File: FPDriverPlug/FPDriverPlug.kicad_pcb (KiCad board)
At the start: 2 copper layers, 21 x 59.1 mm, 3 parts, among them CN1 Conn_02x05_Odd_Even, CN2 Conn_02x20_Counter_Clockwise_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, U1 FP2800A

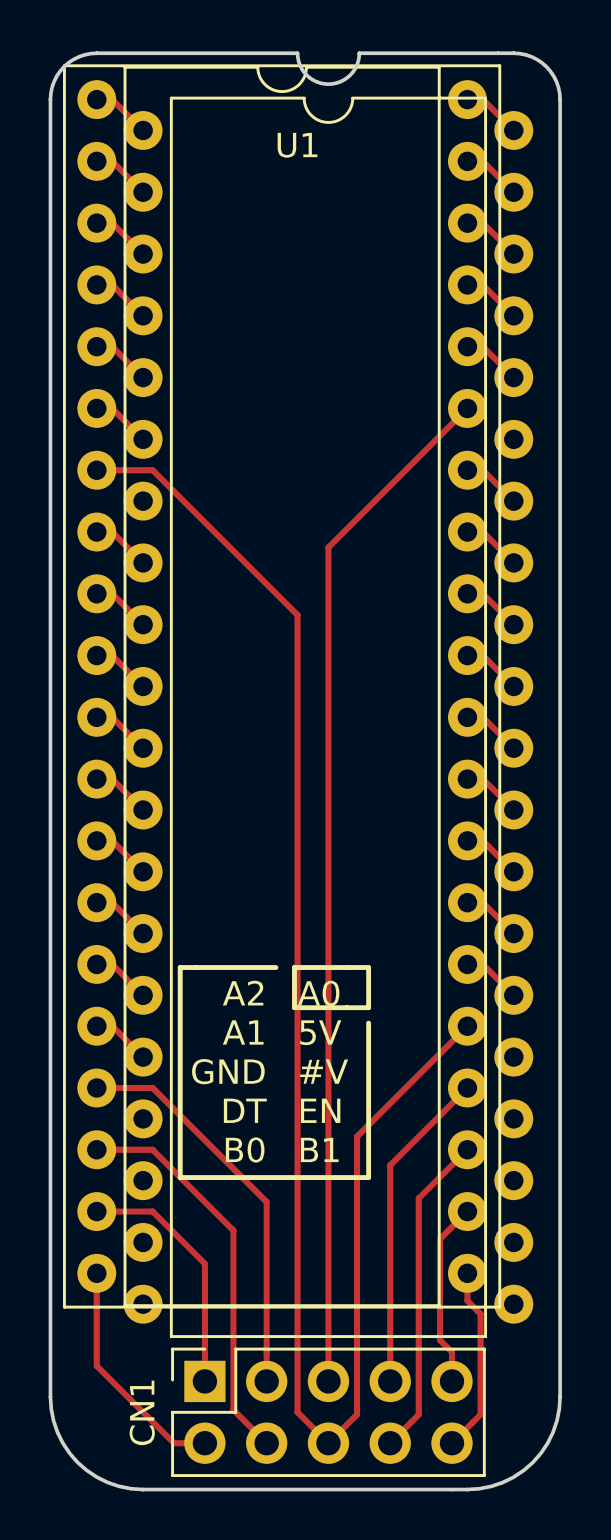
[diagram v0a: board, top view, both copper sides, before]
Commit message: Improve FPDriverPlug
- Switch from DIP40 to DIP32
- Use stronger traces for connections with relevant current
- Use copper fill for GND
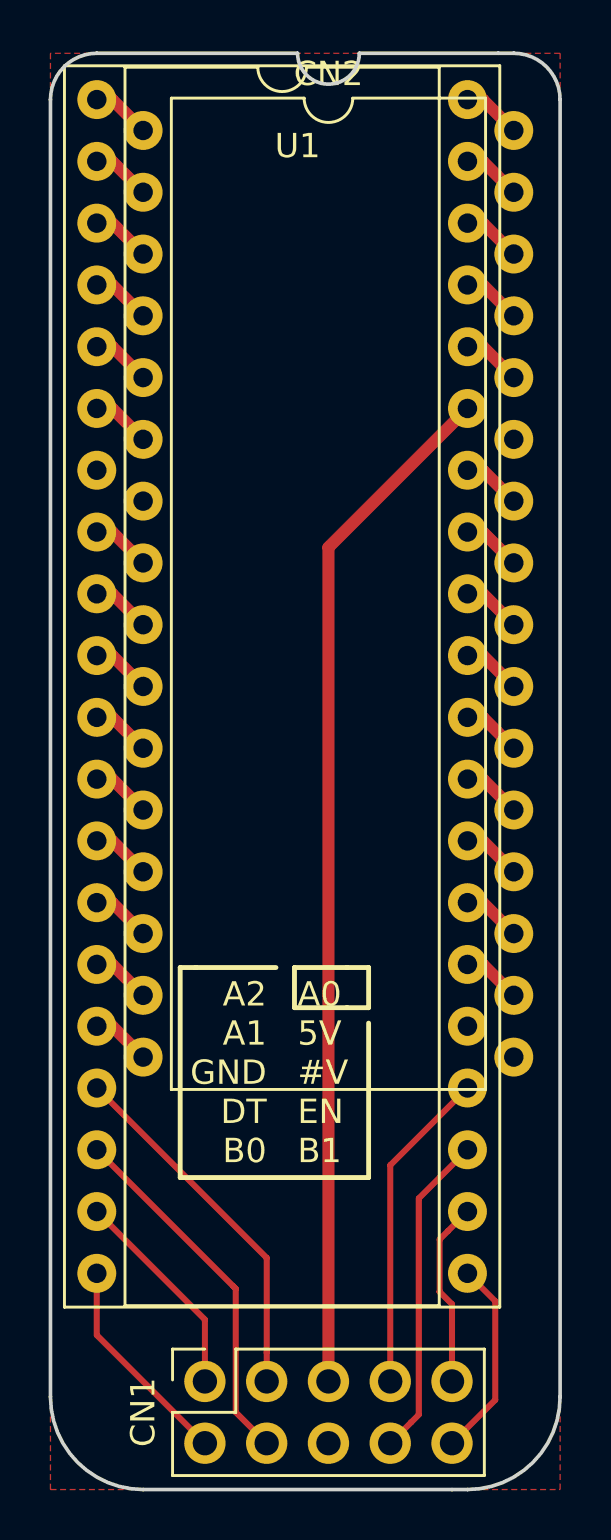
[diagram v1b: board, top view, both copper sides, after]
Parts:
- CN2: value Conn_02x20_Counter_Clockwise_MountingPin -> Conn_02x16_Counter_Clockwise; footprint Housings_DIP:DIP-40_W15.24mm -> Housings_DIP:DIP-32_W15.24mm
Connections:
- U1 pad 26: Net-(CN2-Pad26) -> Net-(CN2-Pad18)
- U1 pad 27: Net-(CN2-Pad27) -> Net-(CN2-Pad19)
- U1 pad 28: Net-(CN2-Pad28) -> Net-(CN2-Pad20)
- U1 pad 29: Net-(CN2-Pad29) -> Net-(CN2-Pad21)
- U1 pad 30: Net-(CN2-Pad30) -> Net-(CN2-Pad22)
- U1 pad 31: Net-(CN2-Pad31) -> Net-(CN2-Pad23)
- U1 pad 32: Net-(CN2-Pad32) -> Net-(CN2-Pad24)
- U1 pad 33: Net-(CN2-Pad33) -> Net-(CN2-Pad25)
- U1 pad 34: Net-(CN2-Pad34) -> Net-(CN2-Pad26)
- U1 pad 36: Net-(CN2-Pad36) -> Net-(CN2-Pad28)
- U1 pad 37: Net-(CN2-Pad37) -> Net-(CN2-Pad29)
- U1 pad 38: Net-(CN2-Pad38) -> Net-(CN2-Pad30)
- U1 pad 39: Net-(CN2-Pad39) -> Net-(CN2-Pad31)
- U1 pad 40: Net-(CN2-Pad40) -> Net-(CN2-Pad32)
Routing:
- net GND: track 64.8 -> 0.00 mm
- net Net-(CN2-Pad38): track 2.43 -> 0.00 mm
- net Net-(CN2-Pad36): track 2.43 -> 0.00 mm
- net Net-(CN2-Pad27): track 2.43 -> 0.00 mm
- net Net-(CN2-Pad23): track 0.00 -> 2.43 mm
- net Net-(CN2-Pad21): track 0.00 -> 2.43 mm
- net Net-(CN2-Pad19): track 0.00 -> 2.43 mm
- net Net-(CN2-Pad40): track 2.43 -> 0.00 mm
- net Net-(CN2-Pad39): track 2.43 -> 0.00 mm
- net Net-(CN2-Pad37): track 2.43 -> 0.00 mm
- net Net-(CN2-Pad34): track 2.43 -> 0.00 mm
- net Net-(CN2-Pad33): track 2.43 -> 0.00 mm
- net Net-(CN2-Pad25): track 0.00 -> 2.43 mm
- net Net-(CN2-Pad24): track 0.00 -> 2.43 mm
- net Net-(CN2-Pad22): track 0.00 -> 2.43 mm
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- added copper zone on F.Cu, net GND
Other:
- net class driver: trace_width 1 -> 0.5
